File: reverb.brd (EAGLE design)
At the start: 152.4 x 25.4 mm, 70 parts, among them IC2 TL074, IC2_EQ1 NE5532, IC4_DRV_RCVR TL072, T1 2N3904

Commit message: have both the drive parts roughly layed out
spring and brick
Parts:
- moved R24 181.5 mm to (74.9, 3.81)
- moved R23 172.7 mm to (82.5, 12.7), turned to 270 degrees
- moved R22 158.3 mm to (78.7, 12.7), turned to 270 degrees
- moved R21 137.8 mm to (59.7, 3.81), turned to 180 degrees
- moved R18 116.9 mm to (59.7, 7.62), turned to 180 degrees
- moved U$22 100.0 mm to (67.3, 6.35), turned to 180 degrees
- moved BRICK 48.3 mm to (71.1, 11.4)
- moved 78L05 44.1 mm to (61.0, 12.7)
- moved IC2 37.0 mm to (119.4, 41.9)
- moved LDR1 25.7 mm to (120.7, 59.7)
- moved REV_SEL 10.2 mm to (90.2, 12.7), turned to 270 degrees
- moved C2 3.81 mm to (102.9, 7.62)
- moved C3 3.81 mm to (104.1, 17.8)
- moved C8 3.81 mm to (120.7, 5.08)
- moved C9 3.81 mm to (119.4, 17.8)
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
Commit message: got some of the EQ rough layout in
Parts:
- moved C7 152.9 mm to (57.1, 67.3)
- moved TILT_EQ10K 150.3 mm to (63.5, 61.0), turned to 90 degrees
- moved R15 131.7 mm to (43.2, 50.8), turned to 180 degrees
- moved R14 130.9 mm to (57.1, 58.4), turned to 270 degrees
- moved C6 125.7 mm to (34.3, 58.4), turned to 270 degrees
- moved R13 103.4 mm to (44.5, 71.1)
- moved R19 83.9 mm to (50.8, 61.0)
- moved R20 81.2 mm to (44.5, 66.0)
- moved R12 78.7 mm to (30.5, 66.0)
- moved IC2 69.9 mm to (55.9, 12.7)
- moved C13 69.6 mm to (41.9, 48.3)
- moved IC2_EQ1 46.0 mm to (41.9, 58.4)
- moved U$22 40.5 mm to (88.9, 40.6)
- moved R18 38.1 mm to (97.8, 6.35), turned to 0 degrees
- moved R21 38.1 mm to (97.8, 2.54), turned to 0 degrees
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
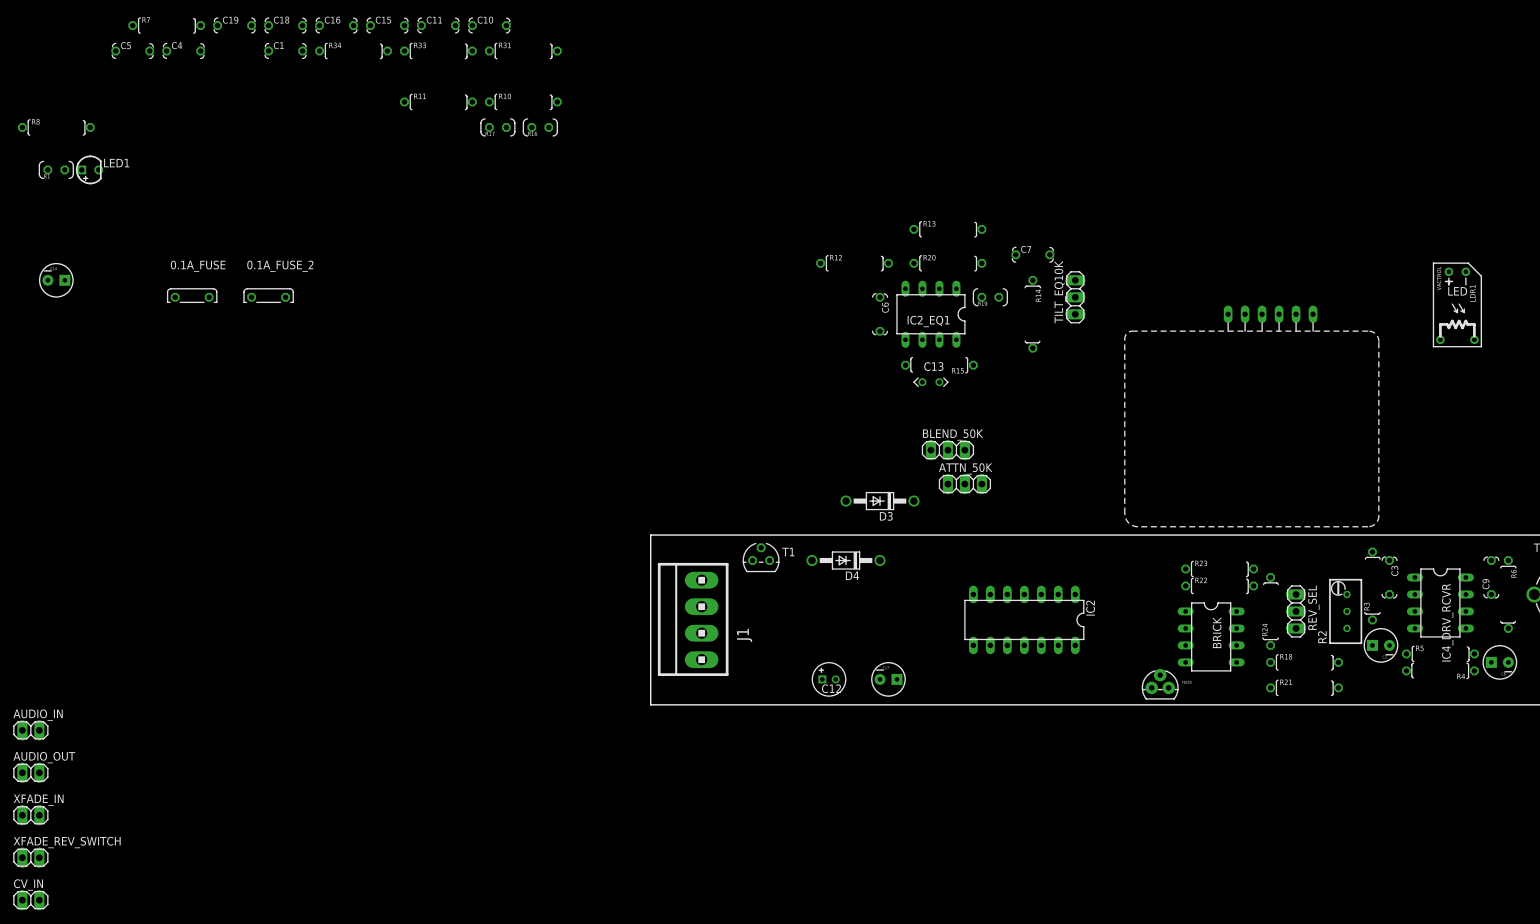
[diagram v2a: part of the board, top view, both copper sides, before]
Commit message: fixed multiple power busses, ditched selection jumpers, layed out more board
selection jumpers: we're just gonna ditch part of the schematic anyways
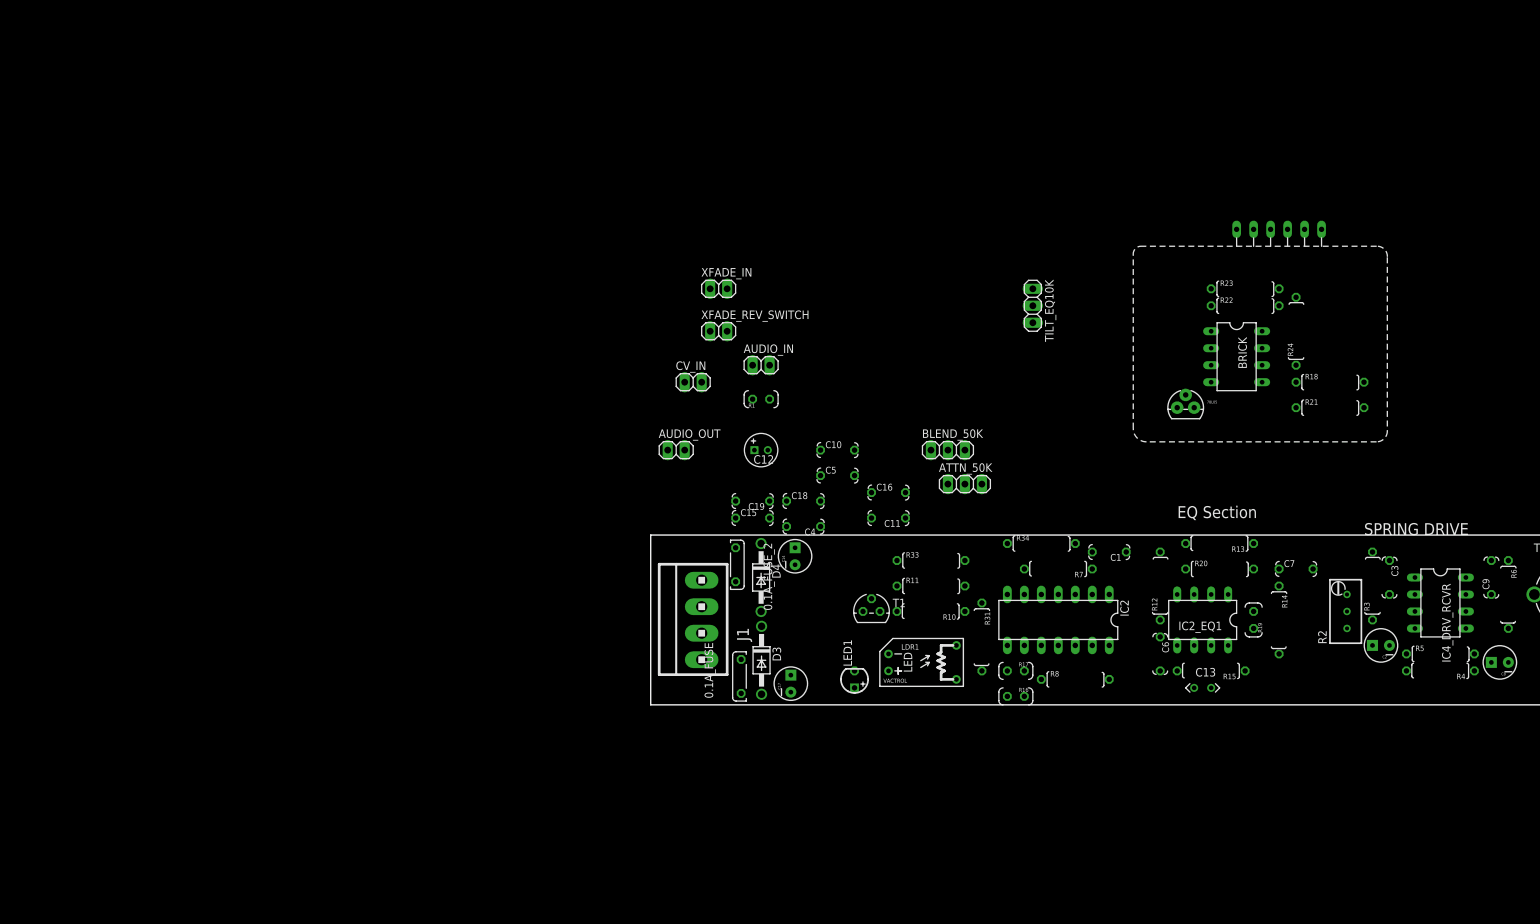
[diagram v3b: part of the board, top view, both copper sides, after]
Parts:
- removed REV_SEL: (no value), pinhead:1X03
- moved R8 173.3 mm to (63.5, 3.81)
- moved R7 156.2 mm to (61.0, 20.3), turned to 180 degrees
- moved C1 144.2 mm to (68.6, 22.9), turned to 180 degrees
- moved LED1 137.4 mm to (30.5, 3.81), turned to 90 degrees
- moved XFADE_IN 129.5 mm to (10.2, 62.2)
- moved XFADE_REV_SWITCH 129.5 mm to (10.2, 55.9)
- moved R34 126.5 mm to (58.4, 24.1)
- moved CV_IN 125.8 mm to (6.35, 48.3)
- moved C5 123.1 mm to (27.9, 34.3)
- moved AUDIO_IN 122.1 mm to (16.5, 50.8)
- moved C14 117.9 mm to (21.6, 22.2), turned to 90 degrees
- moved C4 116.8 mm to (22.9, 26.7), turned to 180 degrees
- moved R17 112.3 mm to (54.6, 5.08), turned to 180 degrees
- moved R31 111.3 mm to (49.5, 10.2), turned to 270 degrees
- moved R16 110.9 mm to (54.6, 1.27), turned to 180 degrees
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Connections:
- removed net -12V: C11.1, C16.2
- removed net N$38: BRICK.7, R24.2, REV_SEL.1
- removed net N$39: C9.2, IC4_DRV_RCVR.7, R6.1, REV_SEL.3
- net +12V: no longer C10.2, C5.2
- net +12V_B: now also C10.2, C5.2
- net -12V_B: now also C11.1, C16.2
- net REVERB_RETURN: now also BRICK.7, C9.2, IC4_DRV_RCVR.7, R24.2, R6.1; no longer REV_SEL.2
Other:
- board text added: "EQ Section"
- board text added: "SPRING DRIVE"

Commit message: moving things around :)
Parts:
- moved C10 35.6 mm to (58.4, 19.7)
- moved C11 31.9 mm to (58.4, 5.71)
- moved R33 9.09 mm to (33.7, 17.8), turned to 90 degrees
- moved R31 8.26 mm to (41.9, 13.3), turned to 0 degrees
- moved R19 8.13 mm to (85.1, 19.1), turned to 180 degrees
- moved C7 7.10 mm to (90.2, 17.1), turned to 90 degrees
- moved T1 4.02 mm to (29.2, 12.7), turned to 270 degrees
- moved LED1 3.24 mm to (31.1, 6.99), turned to 270 degrees
- moved R17 2.62 mm to (52.1, 5.71)
- moved R10 2.54 mm to (41.9, 16.5)
- moved R20 2.01 mm to (84.5, 22.2)
- moved LDR1 1.91 mm to (40.6, 8.26)
- moved R7 1.91 mm to (61.0, 22.2)
- moved R16 1.27 mm to (54.6, 2.54)
- moved R8 1.27 mm to (63.5, 2.54)
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
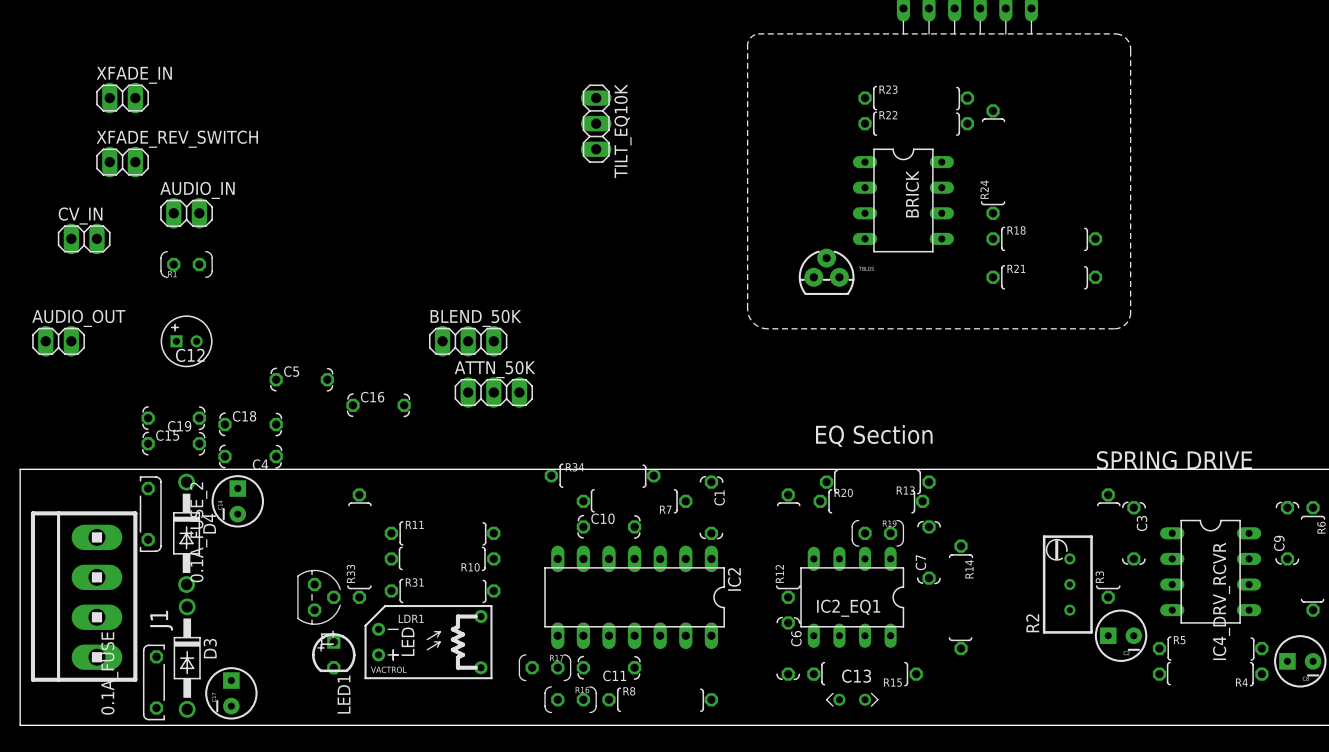
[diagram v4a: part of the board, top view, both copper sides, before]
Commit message: everything should be on the board, just need to move it around
gonna ditch brick section soon, detached it
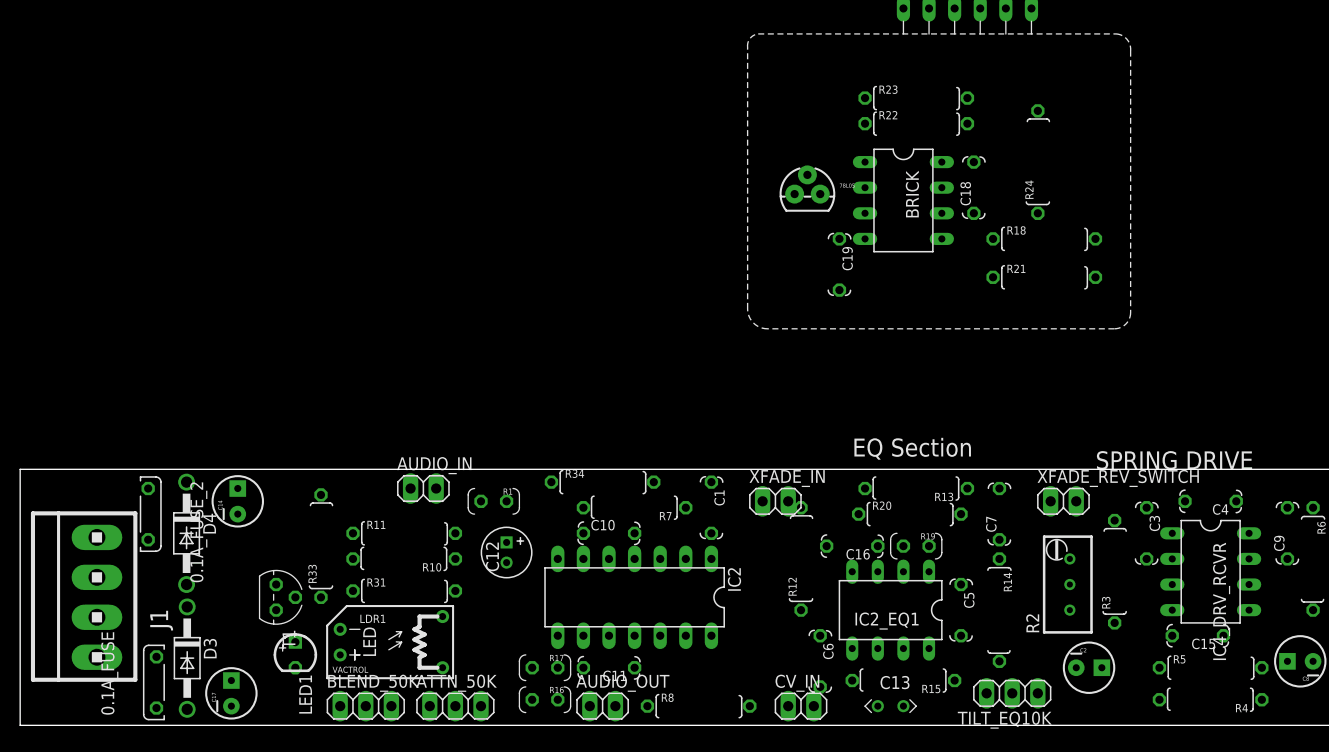
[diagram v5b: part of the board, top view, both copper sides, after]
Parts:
- moved C15 103.4 mm to (116.8, 8.89), turned to 180 degrees
- moved XFADE_REV_SWITCH 99.2 mm to (103.5, 22.2)
- moved C4 95.4 mm to (118.1, 22.2)
- moved CV_IN 84.9 mm to (77.5, 1.91)
- moved XFADE_IN 76.1 mm to (74.9, 22.2)
- moved C18 75.5 mm to (94.6, 53.3), turned to 90 degrees
- moved TILT_EQ10K 70.0 mm to (98.4, 3.17), turned to 180 degrees
- moved C5 69.3 mm to (93.3, 11.4), turned to 270 degrees
- moved C19 67.8 mm to (81.3, 45.7), turned to 270 degrees
- moved AUDIO_OUT 65.0 mm to (57.8, 1.91)
- moved C16 49.0 mm to (82.5, 17.8), turned to 180 degrees
- moved R1 38.5 mm to (47.0, 22.2), turned to 180 degrees
- moved C12 38.0 mm to (48.3, 17.1), turned to 270 degrees
- moved BLEND_50K 37.6 mm to (34.3, 1.91)
- moved AUDIO_IN 36.0 mm to (40.0, 23.5)
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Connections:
- new net BRICKREVERB_SEND: R22.1
- new net BRICK_REVERB_RETURN: BRICK.7, R24.2
- net REVERB_RETURN: no longer BRICK.7, R24.2
- net REVERB_SEND: no longer R22.1

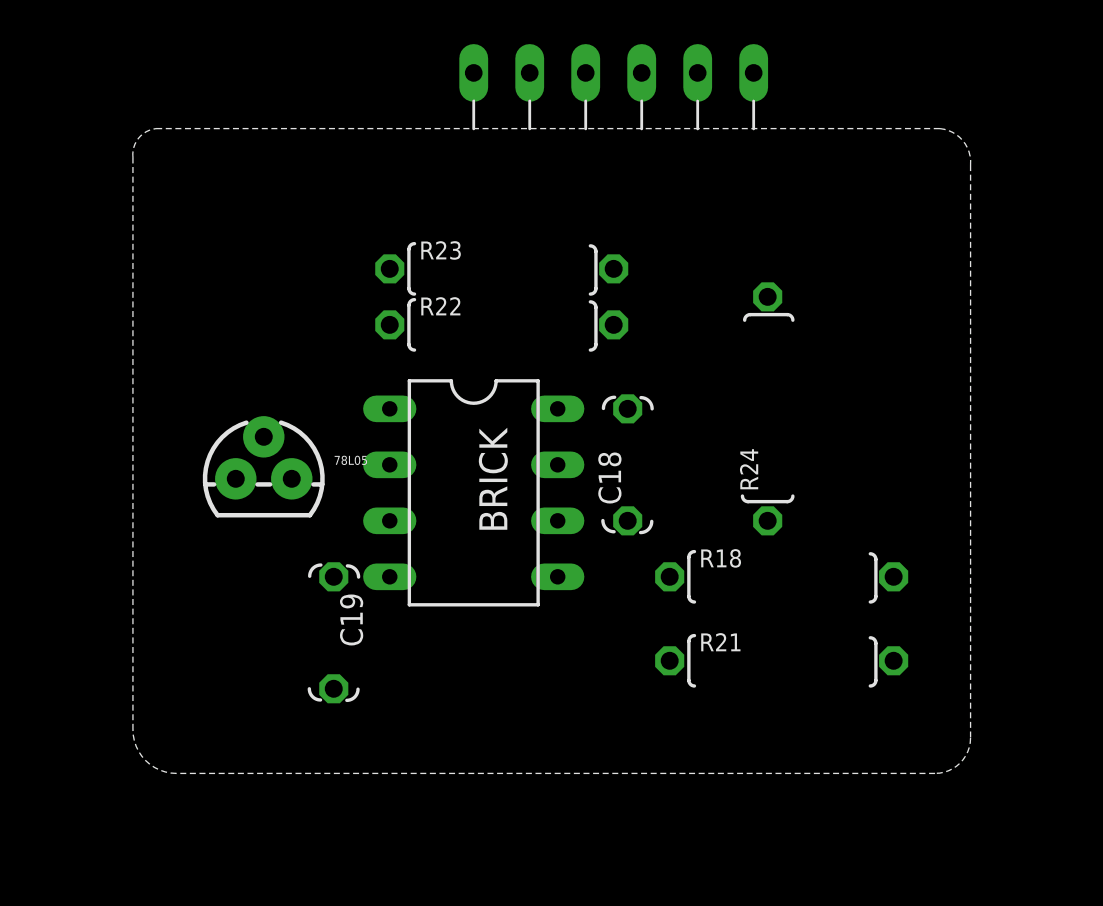
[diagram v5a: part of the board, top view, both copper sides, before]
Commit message: ditched brick section
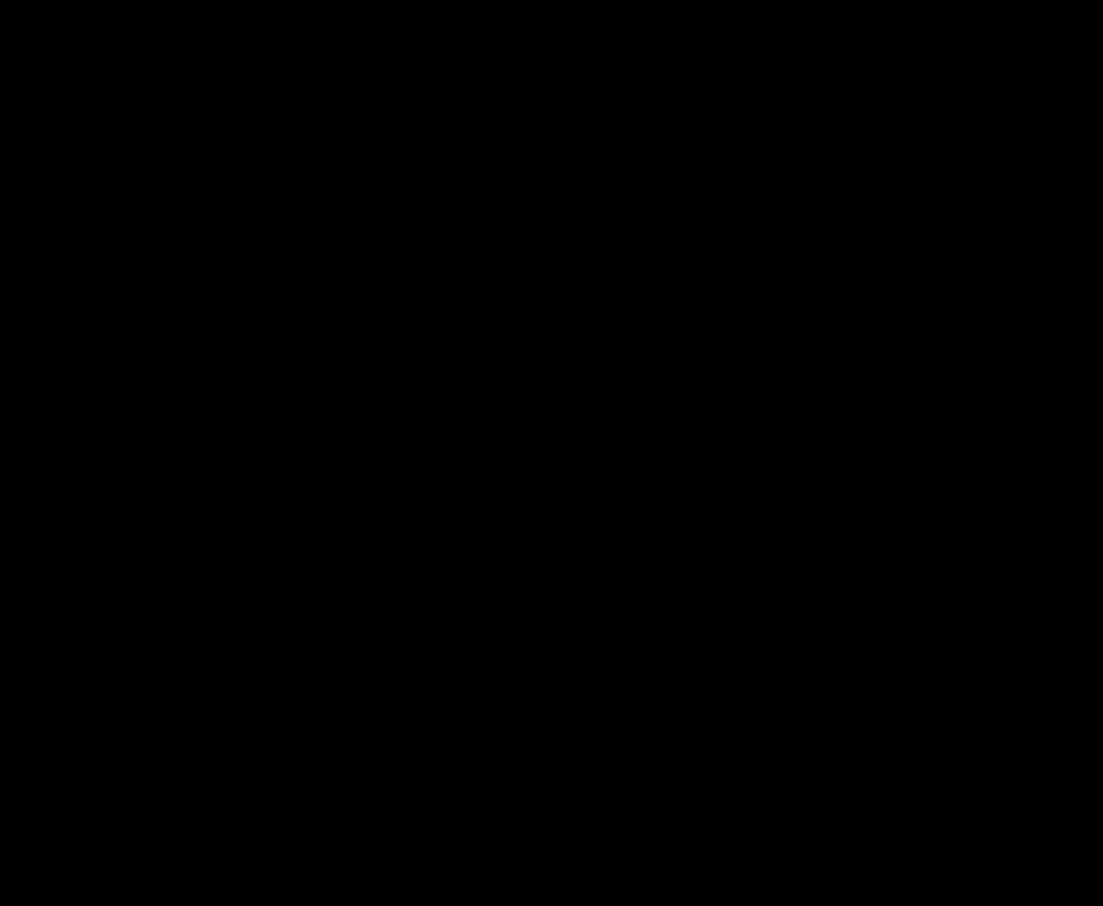
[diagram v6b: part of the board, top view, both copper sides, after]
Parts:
- removed 78L05: (no value), SparkFun-PowerIC:TO-92
- removed BRICK: TL072, TomW:DIL08
- removed C18, C19: 100n, TomW:C050-024X044
- removed R18, R21: 10k, TomW:0207/10
- removed R22: 22k, TomW:0207/10
- removed R23: 2.2k, TomW:0207/10
- removed R24: 68k, TomW:0207/10
- removed U$22: (no value), Accutronics BTDR-2H:BTDR-2H
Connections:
- removed net BRICKREVERB_SEND: R22.1
- removed net BRICK_REVERB_RETURN: BRICK.7, R24.2
- removed net N$19: 78L05.1, U$22.1
- removed net N$27: R22.2, R23.2, U$22.3
- removed net N$28: R18.2, U$22.6
- removed net N$29: R21.2, U$22.5
- removed net N$30: BRICK.6, R18.1, R21.1, R24.1
- removed net N$32: 78L05.2, U$22.2
- removed net N$34: BRICK.1, BRICK.2
- net +12V_B: no longer 78L05.3, BRICK.8, C18.2
- net -12V_B: no longer BRICK.4, C19.1
- net GND_B: no longer BRICK.3, BRICK.5, C18.1, C19.2, R23.1, U$22.4

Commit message: almost layed out, almost ready for routing!
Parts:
- moved CV_IN 31.8 mm to (45.7, 1.91)
- moved BLEND_50K 22.0 mm to (29.8, 23.5)
- moved C12 5.68 mm to (45.7, 22.2), turned to 180 degrees
- moved R33 5.39 mm to (26.0, 14.0)
- moved ATTN_50K 5.08 mm to (38.1, 1.91), turned to 180 degrees
- moved T1 4.45 mm to (21.0, 12.7)
- moved R1 3.70 mm to (50.2, 20.3), turned to 270 degrees
- moved LED1 2.62 mm to (27.9, 4.45), turned to 90 degrees
- moved XFADE_REV_SWITCH 2.29 mm to (101.6, 23.5)
- moved XFADE_IN 1.80 mm to (73.7, 23.5)
- moved AUDIO_IN 0.64 mm to (39.4, 23.5), turned to 180 degrees
- moved C8 0.64 mm to (127.6, 6.35), turned to 270 degrees
- moved R10 0.64 mm to (38.1, 15.9)
- moved R11 0.64 mm to (38.1, 18.4)
- moved C6 0.64 mm to (79.4, 6.99)
